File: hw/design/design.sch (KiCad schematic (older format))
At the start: 0 parts

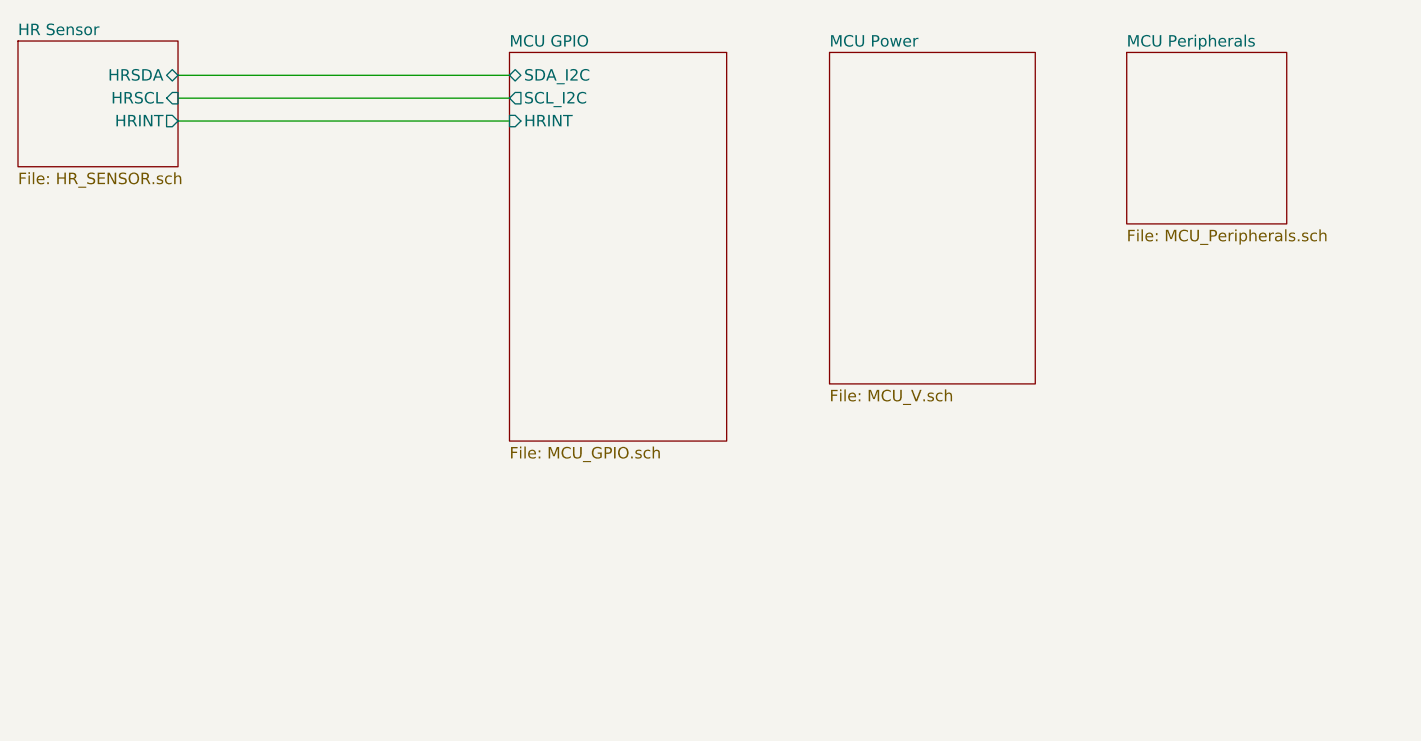
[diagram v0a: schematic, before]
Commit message: schematic/parts: SD Card
I have elected to move from writing notes to writing git commits instead. It may be easier to read for some.
Anyhow, I decided to research a little bit for a thinner SD card mount to improve my odds of the HR sensor being the tallest part on one side of the PCB.
Quite unlikely, but still. Didn't take much time at all and had to do some digging around for how the SD spec even works electronically.
Notes file will still keep track of all the parts, I might rename the file to "parts" as that's its most useful case other than me thinking on pixel.

Still workin'
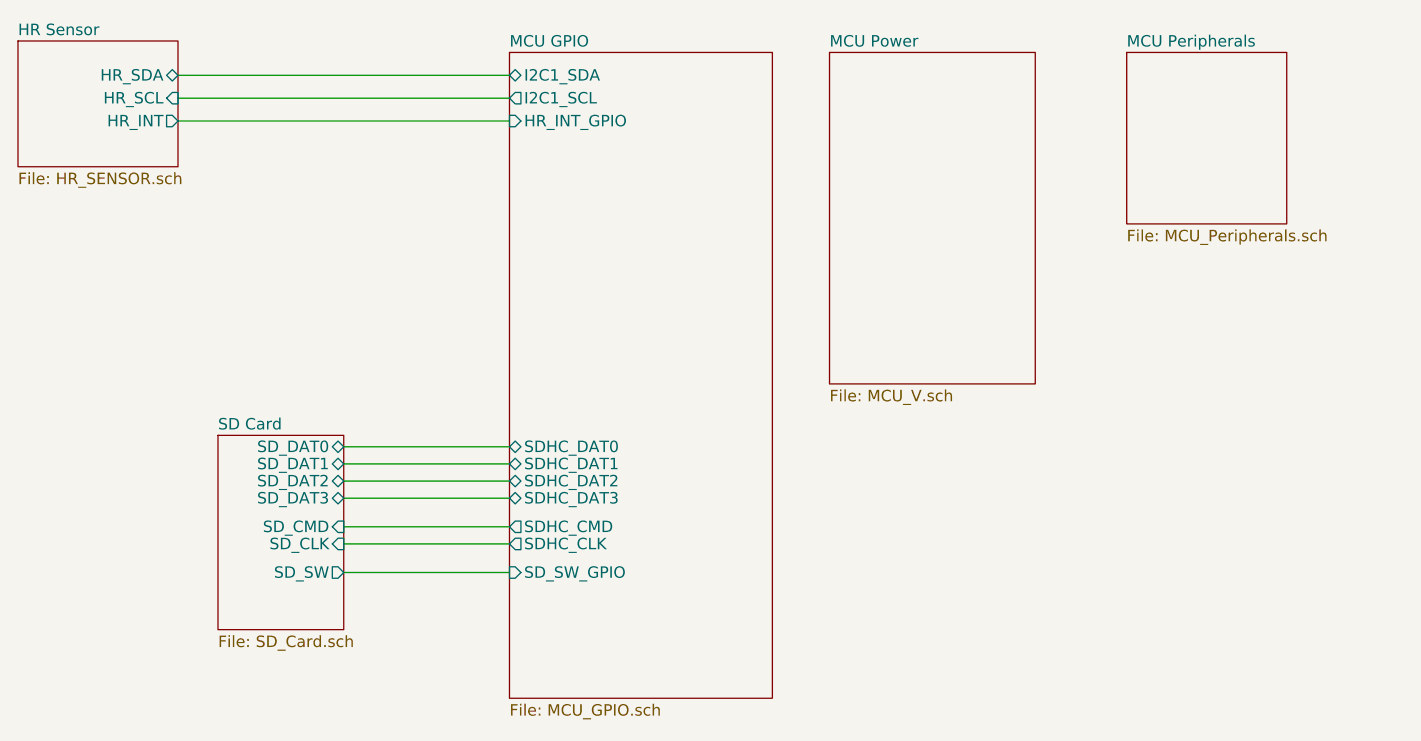
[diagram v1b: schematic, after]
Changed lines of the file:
@@
 $Descr A4 11693 8268
 encoding utf-8
-Sheet 1 5
+Sheet 1 6
 Title ""
 Date ""
@@
 F0 "HR Sensor" 50
 F1 "HR_SENSOR.sch" 50
-F2 "HRSDA" B R 2650 1400 50
-F3 "HRSCL" I R 2650 1500 50
-F4 "HRINT" O R 2650 1600 50
+F2 "HR_SDA" B R 2650 1400 50
+F3 "HR_SCL" I R 2650 1500 50
+F4 "HR_INT" O R 2650 1600 50
 $EndSheet
 Wire Wire Line
@@
 Wire Wire Line
 	2650 1600 4100 1600
-$Sheet
-S 4100 1300 950  1700
-U 5E117560
-F0 "MCU GPIO" 50
-F1 "MCU_GPIO.sch" 50
-F2 "HRINT" I L 4100 1600 50
-F3 "SDA_I2C" B L 4100 1400 50
-F4 "SCL_I2C" O L 4100 1500 50
-$EndSheet
 $Sheet
 S 5500 1300 900  1450
@@
 F1 "MCU_Peripherals.sch" 50
 $EndSheet
+$Sheet
+S 2825 2975 550  850
+U 5E180B58
+F0 "SD Card" 50
+F1 "SD_Card.sch" 50
+F2 "SD_DAT1" B R 3375 3100 50
+F3 "SD_DAT0" B R 3375 3025 50
+F4 "SD_DAT2" B R 3375 3175 50
+F5 "SD_DAT3" B R 3375 3250 50
+F6 "SD_CMD" I R 3375 3375 50
+F7 "SD_CLK" I R 3375 3450 50
+F9 "SD_SW" O R 3375 3575 50
+$EndSheet
+$Sheet
+S 4100 1300 1150 2825
+U 5E117560
+F0 "MCU GPIO" 50
+F1 "MCU_GPIO.sch" 50
+F2 "HR_INT_GPIO" I L 4100 1600 50
+F3 "I2C1_SDA" B L 4100 1400 50
+F4 "I2C1_SCL" O L 4100 1500 50
+F5 "SD_SW_GPIO" I L 4100 3575 50
+F6 "SDHC_DAT0" B L 4100 3025 50
+F7 "SDHC_CLK" O L 4100 3450 50
+F8 "SDHC_DAT1" B L 4100 3100 50
+F9 "SDHC_DAT3" B L 4100 3250 50
+F10 "SDHC_CMD" O L 4100 3375 50
+F11 "SDHC_DAT2" B L 4100 3175 50
+$EndSheet
+Wire Wire Line
+	4100 3025 3375 3025
+Wire Wire Line
+	3375 3100 4100 3100
+Wire Wire Line
+	4100 3175 3375 3175
+Wire Wire Line
+	3375 3250 4100 3250
+Wire Wire Line
+	3375 3375 4100 3375
+Wire Wire Line
+	3375 3450 4100 3450
+Wire Wire Line
+	3375 3575 4100 3575
 $EndSCHEMATC
